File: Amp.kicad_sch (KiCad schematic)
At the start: 13 parts, among them U4 MCP6004

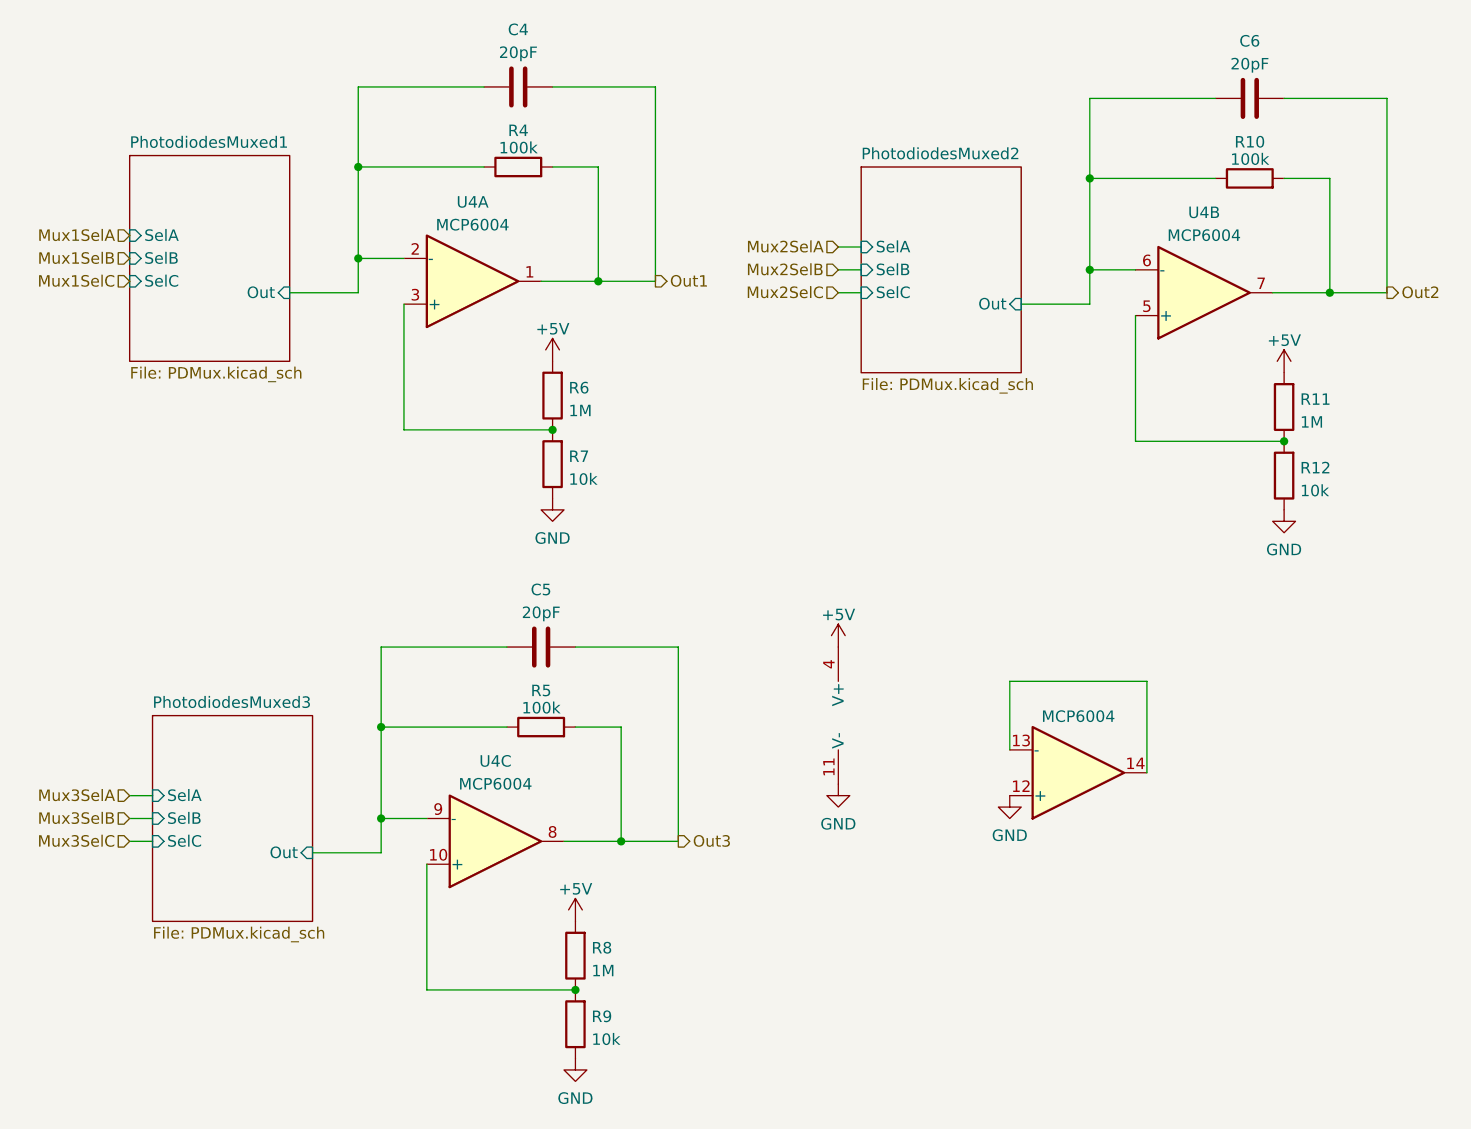
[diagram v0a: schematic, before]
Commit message: Added photodiode connector, haven't routed
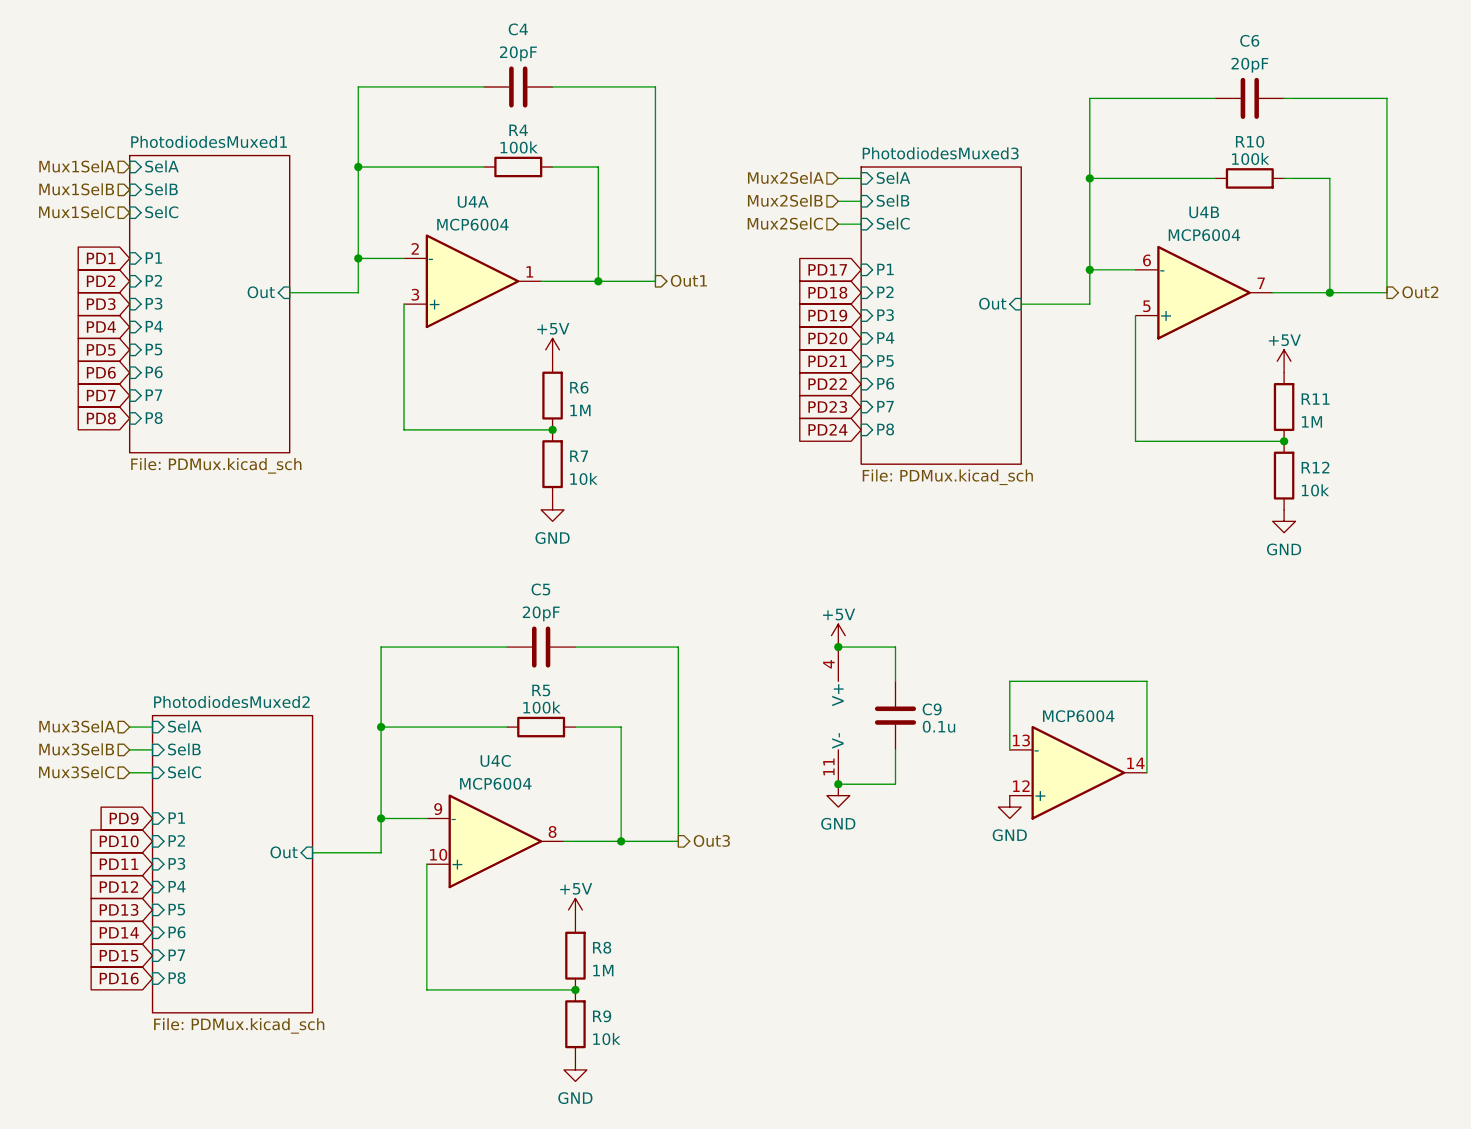
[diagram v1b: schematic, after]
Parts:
- added C9: 0.1u, symbol Device:C
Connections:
- net +5V: now also C9.1
- net GND: now also C9.2
- net PhotodiodesMuxed2/Out: now also C5.1, R5.1, U4.9 (-); no longer C6.1, R10.1, U4.6 (-)
- net PhotodiodesMuxed3/Out: now also C6.1, R10.1, U4.6 (-); no longer C5.1, R5.1, U4.9 (-)
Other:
- sheet PhotodiodesMuxed1 ports: added P1, P2, P3, P4, P5, P6, P7, P8; removed none
- sheet PhotodiodesMuxed2 ports: added P1, P2, P3, P4, P5, P6, P7, P8; removed none
- sheet PhotodiodesMuxed3 ports: added P1, P2, P3, P4, P5, P6, P7, P8; removed none

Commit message: Add connectors, routed
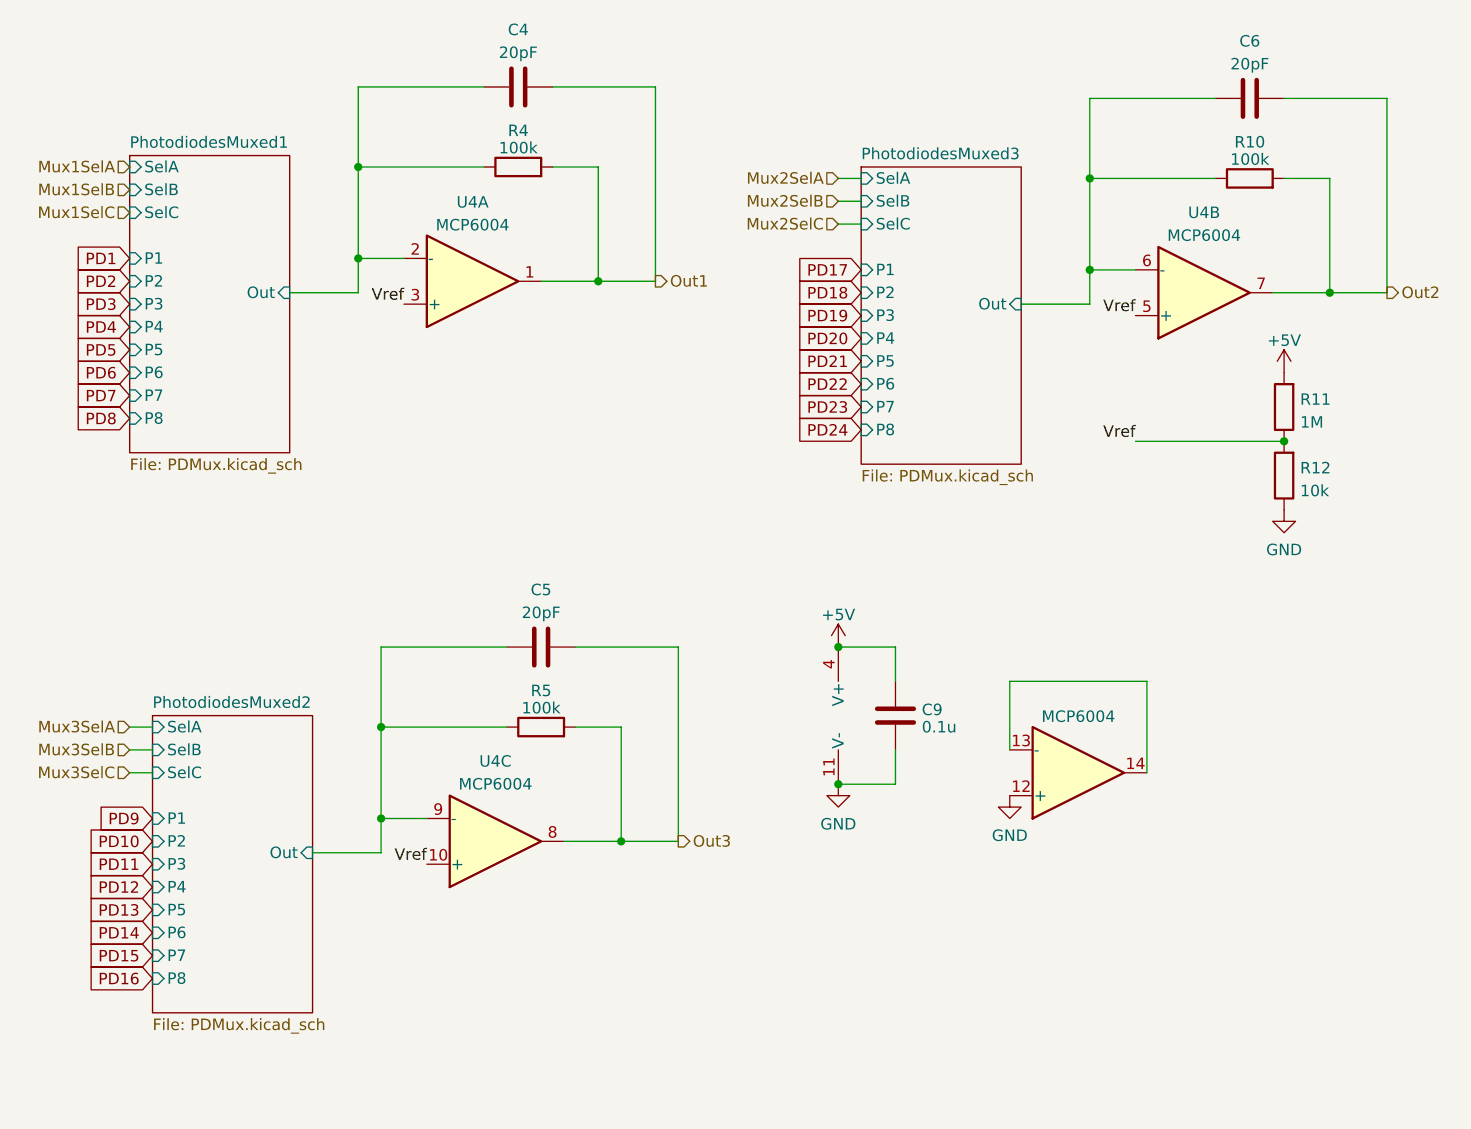
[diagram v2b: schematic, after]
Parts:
- removed R6, R8: 1M, Resistor_THT:R_Axial_DIN0204_L3.6mm_D1.6mm_P5.08mm_Horizontal, symbol Device:R
- removed R7, R9: 10k, Resistor_THT:R_Axial_DIN0204_L3.6mm_D1.6mm_P5.08mm_Horizontal, symbol Device:R
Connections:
- net Vref: now reaches U4.10 (+)
- net Vref: now also R11.1, R12.2, U4.3 (+), U4.5 (+)
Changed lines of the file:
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@@
   (junction (at 78.74 29.21) (diameter 0) (color 0 0 0 0)
   )
-  (junction (at 102.87 120.65) (diameter 0) (color 0 0 0 0)
-  )
   (junction (at 81.28 101.6) (diameter 0) (color 0 0 0 0)
   )
-  (junction (at 100.33 58.42) (diameter 0) (color 0 0 0 0)
-  )
   (junction (at 81.28 91.44) (diameter 0) (color 0 0 0 0)
   )
@@
     (stroke (width 0) (type default))
   )
-  (wire (pts (xy 83.82 58.42) (xy 83.82 44.45))
-    (stroke (width 0) (type default))
-  )
   (wire (pts (xy 100.33 20.32) (xy 111.76 20.32))
     (stroke (width 0) (type default))
@@
     (stroke (width 0) (type default))
   )
-  (wire (pts (xy 86.36 120.65) (xy 102.87 120.65))
-    (stroke (width 0) (type default))
-  )
   (wire (pts (xy 166.37 96.52) (xy 166.37 86.36))
     (stroke (width 0) (type default))
@@
     (stroke (width 0) (type default))
   )
-  (wire (pts (xy 86.36 120.65) (xy 86.36 106.68))
-    (stroke (width 0) (type default))
-  )
   (wire (pts (xy 102.87 82.55) (xy 114.3 82.55))
     (stroke (width 0) (type default))
@@
     (stroke (width 0) (type default))
   )
-  (wire (pts (xy 83.82 58.42) (xy 100.33 58.42))
-    (stroke (width 0) (type default))
-  )
   (wire (pts (xy 180.34 43.18) (xy 186.69 43.18))
     (stroke (width 0) (type default))
@@
     (stroke (width 0) (type default))
   )
-  (wire (pts (xy 165.1 59.69) (xy 165.1 45.72))
-    (stroke (width 0) (type default))
-  )
   (wire (pts (xy 181.61 21.59) (xy 193.04 21.59))
     (stroke (width 0) (type default))
+  )
+  (label "Vref" (at 165.1 59.69 180) (fields_autoplaced)
+    (effects (font (size 1.27 1.27)) (justify right bottom))
+  )
+  (label "Vref" (at 165.1 45.72 180) (fields_autoplaced)
+    (effects (font (size 1.27 1.27)) (justify right bottom))
+  )
+  (label "Vref" (at 86.36 106.68 180) (fields_autoplaced)
+    (effects (font (size 1.27 1.27)) (justify right bottom))
+  )
+  (label "Vref" (at 83.82 44.45 180) (fields_autoplaced)
+    (effects (font (size 1.27 1.27)) (justify right bottom))
   )
   (global_label "PD18" (shape input) (at 134.62 43.18 180) (fields_autoplaced)
@@
         (path "/733e9294-e088-4082-934a-063f4ef007c2/827b7f4c-5327-4808-a7a4-ad3ee80b03f3"
           (reference "R4") (unit 1)
-        )
-      )
-    )
-  )
-  (symbol (lib_id "Device:R") (at 102.87 124.46 180) (unit 1)
-    (in_bom yes) (on_board yes) (dnp no) (fields_autoplaced)
-    (property "Reference" "R9" (at 104.648 123.6253 0)
-      (effects (font (size 1.27 1.27)) (justify right))
-    )
-    (property "Value" "10k" (at 104.648 126.1622 0)
-      (effects (font (size 1.27 1.27)) (justify right))
-    )
-    (property "Footprint" "Resistor_THT:R_Axial_DIN0204_L3.6mm_D1.6mm_P5.08mm_Horizontal" (at 104.648 124.46 90)
-      (effects (font (size 1.27 1.27)) hide)
-    )
-    (property "Datasheet" "~" (at 102.87 124.46 0)
-      (effects (font (size 1.27 1.27)) hide)
-    )
-    (pin "1")
-    (pin "2")
-    (instances
-      (project "photodiode_jasmine"
-        (path "/733e9294-e088-4082-934a-063f4ef007c2/827b7f4c-5327-4808-a7a4-ad3ee80b03f3"
-          (reference "R9") (unit 1)
         )
       )
@@
     )
   )
-  (symbol (lib_id "power:+5V") (at 102.87 113.03 0) (unit 1)
-    (in_bom yes) (on_board yes) (dnp no) (fields_autoplaced)
-    (property "Reference" "#PWR024" (at 102.87 116.84 0)
-      (effects (font (size 1.27 1.27)) hide)
-    )
-    (property "Value" "+5V" (at 102.87 109.4542 0)
-      (effects (font (size 1.27 1.27)))
-    )
-    (property "Footprint" "" (at 102.87 113.03 0)
-      (effects (font (size 1.27 1.27)) hide)
-    )
-    (property "Datasheet" "" (at 102.87 113.03 0)
-      (effects (font (size 1.27 1.27)) hide)
-    )
-    (pin "1")
-    (instances
-      (project "photodiode_jasmine"
-        (path "/733e9294-e088-4082-934a-063f4ef007c2/827b7f4c-5327-4808-a7a4-ad3ee80b03f3"
-          (reference "#PWR024") (unit 1)
-        )
-      )
-    )
-  )
   (symbol (lib_id "Device:C") (at 99.06 82.55 90) (unit 1)
     (in_bom yes) (on_board yes) (dnp no) (fields_autoplaced)
@@
         (path "/733e9294-e088-4082-934a-063f4ef007c2/827b7f4c-5327-4808-a7a4-ad3ee80b03f3"
           (reference "#PWR026") (unit 1)
-        )
-      )
-    )
-  )
-  (symbol (lib_id "power:GND") (at 102.87 128.27 0) (unit 1)
-    (in_bom yes) (on_board yes) (dnp no) (fields_autoplaced)
-    (property "Reference" "#PWR025" (at 102.87 134.62 0)
-      (effects (font (size 1.27 1.27)) hide)
-    )
-    (property "Value" "GND" (at 102.87 132.7134 0)
-      (effects (font (size 1.27 1.27)))
-    )
-    (property "Footprint" "" (at 102.87 128.27 0)
-      (effects (font (size 1.27 1.27)) hide)
-    )
-    (property "Datasheet" "" (at 102.87 128.27 0)
-      (effects (font (size 1.27 1.27)) hide)
-    )
-    (pin "1")
-    (instances
-      (project "photodiode_jasmine"
-        (path "/733e9294-e088-4082-934a-063f4ef007c2/827b7f4c-5327-4808-a7a4-ad3ee80b03f3"
-          (reference "#PWR025") (unit 1)
-        )
-      )
-    )
-  )
-  (symbol (lib_id "power:GND") (at 100.33 66.04 0) (unit 1)
-    (in_bom yes) (on_board yes) (dnp no) (fields_autoplaced)
-    (property "Reference" "#PWR023" (at 100.33 72.39 0)
-      (effects (font (size 1.27 1.27)) hide)
-    )
-    (property "Value" "GND" (at 100.33 70.4834 0)
-      (effects (font (size 1.27 1.27)))
-    )
-    (property "Footprint" "" (at 100.33 66.04 0)
-      (effects (font (size 1.27 1.27)) hide)
-    )
-    (property "Datasheet" "" (at 100.33 66.04 0)
-      (effects (font (size 1.27 1.27)) hide)
-    )
-    (pin "1")
-    (instances
-      (project "photodiode_jasmine"
-        (path "/733e9294-e088-4082-934a-063f4ef007c2/827b7f4c-5327-4808-a7a4-ad3ee80b03f3"
-          (reference "#PWR023") (unit 1)
-        )
-      )
-    )
-  )
-  (symbol (lib_id "Device:R") (at 100.33 62.23 180) (unit 1)
-    (in_bom yes) (on_board yes) (dnp no) (fields_autoplaced)
-    (property "Reference" "R7" (at 102.108 61.3953 0)
-      (effects (font (size 1.27 1.27)) (justify right))
-    )
-    (property "Value" "10k" (at 102.108 63.9322 0)
-      (effects (font (size 1.27 1.27)) (justify right))
-    )
-    (property "Footprint" "Resistor_THT:R_Axial_DIN0204_L3.6mm_D1.6mm_P5.08mm_Horizontal" (at 102.108 62.23 90)
-      (effects (font (size 1.27 1.27)) hide)
-    )
-    (property "Datasheet" "~" (at 100.33 62.23 0)
-      (effects (font (size 1.27 1.27)) hide)
-    )
-    (pin "1")
-    (pin "2")
-    (instances
-      (project "photodiode_jasmine"
-        (path "/733e9294-e088-4082-934a-063f4ef007c2/827b7f4c-5327-4808-a7a4-ad3ee80b03f3"
-          (reference "R7") (unit 1)
-        )
-      )
-    )
-  )
-  (symbol (lib_id "Device:R") (at 102.87 116.84 180) (unit 1)
-    (in_bom yes) (on_board yes) (dnp no) (fields_autoplaced)
-    (property "Reference" "R8" (at 104.648 116.0053 0)
-      (effects (font (size 1.27 1.27)) (justify right))
-    )
-    (property "Value" "1M" (at 104.648 118.5422 0)
-      (effects (font (size 1.27 1.27)) (justify right))
-    )
-    (property "Footprint" "Resistor_THT:R_Axial_DIN0204_L3.6mm_D1.6mm_P5.08mm_Horizontal" (at 104.648 116.84 90)
-      (effects (font (size 1.27 1.27)) hide)
-    )
-    (property "Datasheet" "~" (at 102.87 116.84 0)
-      (effects (font (size 1.27 1.27)) hide)
-    )
-    (pin "1")
-    (pin "2")
-    (instances
-      (project "photodiode_jasmine"
-        (path "/733e9294-e088-4082-934a-063f4ef007c2/827b7f4c-5327-4808-a7a4-ad3ee80b03f3"
-          (reference "R8") (unit 1)
-        )
-      )
-    )
-  )
-  (symbol (lib_id "power:+5V") (at 100.33 50.8 0) (unit 1)
-    (in_bom yes) (on_board yes) (dnp no) (fields_autoplaced)
-    (property "Reference" "#PWR022" (at 100.33 54.61 0)
-      (effects (font (size 1.27 1.27)) hide)
-    )
-    (property "Value" "+5V" (at 100.33 47.2242 0)
-      (effects (font (size 1.27 1.27)))
-    )
-    (property "Footprint" "" (at 100.33 50.8 0)
-      (effects (font (size 1.27 1.27)) hide)
-    )
-    (property "Datasheet" "" (at 100.33 50.8 0)
-      (effects (font (size 1.27 1.27)) hide)
-    )
-    (pin "1")
-    (instances
-      (project "photodiode_jasmine"
-        (path "/733e9294-e088-4082-934a-063f4ef007c2/827b7f4c-5327-4808-a7a4-ad3ee80b03f3"
-          (reference "#PWR022") (unit 1)
         )
       )
@@
         )
       )
-    )
-  )
-  (symbol (lib_id "Device:R") (at 100.33 54.61 180) (unit 1)
-    (in_bom yes) (on_board yes) (dnp no) (fields_autoplaced)
-    (property "Reference" "R6" (at 102.108 53.7753 0)
-      (effects (font (size 1.27 1.27)) (justify right))
-    )
-    (property "Value" "1M" (at 102.108 56.3122 0)
-      (effects (font (size 1.27 1.27)) (justify right))
-    )
-    (property "Footprint" "Resistor_THT:R_Axial_DIN0204_L3.6mm_D1.6mm_P5.08mm_Horizontal" (at 102.108 54.61 90)
-      (effects (font (size 1.27 1.27)) hide)
-    )
-    (property "Datasheet" "~" (at 100.33 54.61 0)
-      (effects (font (size 1.27 1.27)) hide)
-    )
-    (pin "1")
-    (pin "2")
-    (instances
-      (project "photodiode_jasmine"
-        (path "/733e9294-e088-4082-934a-063f4ef007c2/827b7f4c-5327-4808-a7a4-ad3ee80b03f3"
-          (reference "R6") (unit 1)
-        )
-      )

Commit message: Not sure what's changed
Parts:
- C9: footprint (none) -> Capacitor_THT:C_Disc_D5.1mm_W3.2mm_P5.00mm
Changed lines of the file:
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@@
       (effects (font (size 1.27 1.27)) (justify left))
     )
-    (property "Footprint" "" (at 139.3952 93.98 0)
+    (property "Footprint" "Capacitor_THT:C_Disc_D5.1mm_W3.2mm_P5.00mm" (at 139.3952 93.98 0)
       (effects (font (size 1.27 1.27)) hide)
     )
